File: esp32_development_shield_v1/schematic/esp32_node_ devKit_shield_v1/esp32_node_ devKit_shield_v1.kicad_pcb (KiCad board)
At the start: 2 copper layers, 150 x 80 mm, 41 parts, among them J1 Screw_Terminal_01x02, J10 Screw_Terminal_01x02, J11 Screw_Terminal_01x02, J12 Screw_Terminal_01x02, J13 Screw_Terminal_01x02, J14 Screw_Terminal_01x02, J15 Screw_Terminal_01x02, J16 Screw_Terminal_01x02, J17 Screw_Terminal_01x02, J19 Screw_Terminal_01x02, J2 Conn_02x20_Odd_Even, J20 Screw_Terminal_01x02, J21 Screw_Terminal_01x02, J22 Screw_Terminal_01x02, J23 Screw_Terminal_01x02, J24 Screw_Terminal_01x02, J25 Screw_Terminal_01x02, J26 Screw_Terminal_01x02, J27 Conn_01x04, J28 Conn_01x04, J29 Conn_01x04, J3 Conn_02x20_Odd_Even, J30 Conn_01x04, J31 USB_C_Receptacle_PowerOnly_6P, J4 Conn_01x04, J5 Conn_01x04, J6 Conn_01x04, J7 Conn_01x04, J8 Screw_Terminal_01x02, J9 Screw_Terminal_01x02, U2 AMS1117-3.3

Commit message: *
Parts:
- added J18: Conn_01x18_Pin, Connector_PinSocket_2.54mm:PinSocket_1x18_P2.54mm_Vertical, F.Cu at (116.3, 112.0)
- added J32: Conn_01x18_Pin, Connector_PinSocket_2.54mm:PinSocket_1x18_P2.54mm_Vertical, F.Cu at (116.3, 68.0)
- J2, J3: value Conn_02x20_Odd_Even -> Conn_02x19_Odd_Even; footprint Connector_PinSocket_2.54mm:PinSocket_2x20_P2.54mm_Vertical -> Connector_PinSocket_2.54mm:PinSocket_2x19_P2.54mm_Vertical
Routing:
- net /5V: track 269.3 -> 315.1 mm
- net GND: track 442.1 -> 414.4 mm
- net Net-(J18-Pin_16): track 52.1 -> 79.7 mm
- net Net-(J15-Pin_2): track 30.1 -> 41.4 mm
- net Net-(J15-Pin_1): track 28.6 -> 38.2 mm
- net Net-(J18-Pin_15): track 26.7 -> 36.2 mm
- net Net-(J14-Pin_2): track 26.6 -> 33.3 mm
- net Net-(J18-Pin_14): track 24.7 -> 31.3 mm
- net Net-(J3-Pin_10): track 33.0 -> 38.4 mm
- net Net-(J3-Pin_5): track 40.4 -> 45.6 mm
- net Net-(J18-Pin_13): track 23.6 -> 28.8 mm
- net Net-(J14-Pin_1): track 25.5 -> 30.7 mm
- net Net-(J3-Pin_7): track 35.5 -> 40.4 mm
- net Net-(J3-Pin_3): track 43.0 -> 47.5 mm
- net Net-(J10-Pin_1): track 28.8 -> 32.6 mm
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
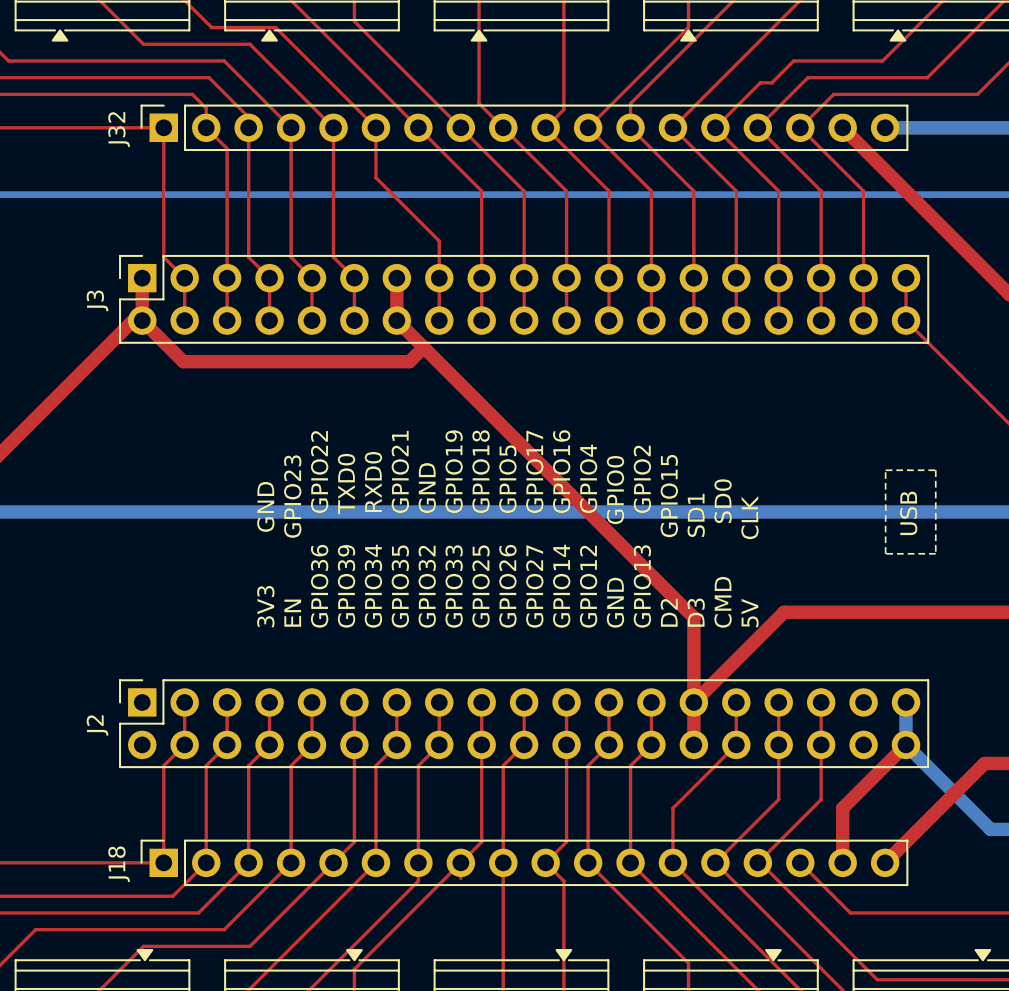
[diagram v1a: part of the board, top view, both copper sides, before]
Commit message: *
Replaced socket with header
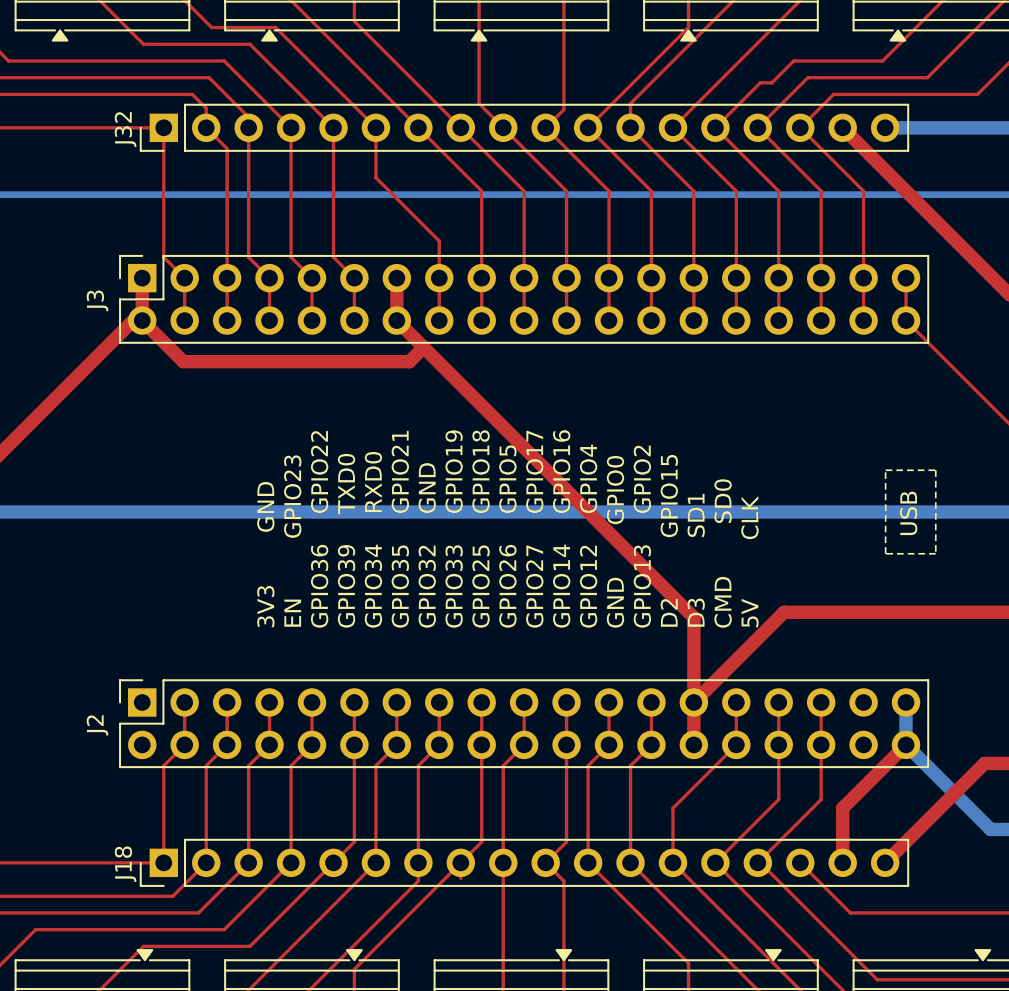
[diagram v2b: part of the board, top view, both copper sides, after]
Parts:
- J18, J32: footprint Connector_PinSocket_2.54mm:PinSocket_1x18_P2.54mm_Vertical -> Connector_PinHeader_2.54mm:PinHeader_1x18_P2.54mm_Vertical
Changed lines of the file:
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@@
 		)
 	)
-	(footprint "Connector_PinSocket_2.54mm:PinSocket_1x18_P2.54mm_Vertical"
+	(footprint "Connector_PinHeader_2.54mm:PinHeader_1x18_P2.54mm_Vertical"
 		(layer "F.Cu")
 		(at 116.29 68 90)
-		(descr "Through hole straight socket strip, 1x18, 2.54mm pitch, single row (from Kicad 4.0.7), script generated")
-		(tags "Through hole socket strip THT 1x18 2.54mm single row")
+		(descr "Through hole straight pin header, 1x18, 2.54mm pitch, single row")
+		(tags "Through hole pin header THT 1x18 2.54mm single row")
 		(property "Reference" "J32"
-			(at 0 -2.77 90)
+			(at 0 -2.38 90)
 			(layer "F.SilkS")
 			(effects
@@
 		)
 		(property "Value" "Conn_01x18_Pin"
-			(at 0 45.95 90)
+			(at 0 45.56 90)
 			(layer "F.Fab")
 			(effects
@@
 		(duplicate_pad_numbers_are_jumpers no)
 		(fp_line
-			(start 1.33 -1.33)
-			(end 1.33 0)
-			(stroke
-				(width 0.12)
-				(type solid)
-			)
-			(layer "F.SilkS")
-		)
-		(fp_line
-			(start 0 -1.33)
-			(end 1.33 -1.33)
-			(stroke
-				(width 0.12)
-				(type solid)
-			)
-			(layer "F.SilkS")
-		)
-		(fp_line
-			(start 1.33 1.27)
-			(end 1.33 44.51)
-			(stroke
-				(width 0.12)
-				(type solid)
-			)
-			(layer "F.SilkS")
-		)
-		(fp_line
-			(start -1.33 1.27)
-			(end 1.33 1.27)
-			(stroke
-				(width 0.12)
-				(type solid)
-			)
-			(layer "F.SilkS")
-		)
-		(fp_line
-			(start -1.33 1.27)
-			(end -1.33 44.51)
-			(stroke
-				(width 0.12)
-				(type solid)
-			)
-			(layer "F.SilkS")
-		)
-		(fp_line
-			(start -1.33 44.51)
-			(end 1.33 44.51)
-			(stroke
-				(width 0.12)
-				(type solid)
-			)
-			(layer "F.SilkS")
-		)
-		(fp_line
-			(start 1.77 -1.77)
+			(start -1.38 -1.38)
+			(end 0 -1.38)
+			(stroke
+				(width 0.12)
+				(type solid)
+			)
+			(layer "F.SilkS")
+		)
+		(fp_line
+			(start -1.38 0)
+			(end -1.38 -1.38)
+			(stroke
+				(width 0.12)
+				(type solid)
+			)
+			(layer "F.SilkS")
+		)
+		(fp_line
+			(start 1.38 1.27)
+			(end 1.38 44.56)
+			(stroke
+				(width 0.12)
+				(type solid)
+			)
+			(layer "F.SilkS")
+		)
+		(fp_line
+			(start -1.38 1.27)
+			(end 1.38 1.27)
+			(stroke
+				(width 0.12)
+				(type solid)
+			)
+			(layer "F.SilkS")
+		)
+		(fp_line
+			(start -1.38 1.27)
+			(end -1.38 44.56)
+			(stroke
+				(width 0.12)
+				(type solid)
+			)
+			(layer "F.SilkS")
+		)
+		(fp_line
+			(start -1.38 44.56)
+			(end 1.38 44.56)
+			(stroke
+				(width 0.12)
+				(type solid)
+			)
+			(layer "F.SilkS")
+		)
+		(fp_rect
+			(start -1.77 -1.78)
 			(end 1.77 44.95)
 			(stroke
@@
 				(type solid)
 			)
+			(fill no)
 			(layer "F.CrtYd")
 		)
 		(fp_line
-			(start -1.77 -1.77)
-			(end 1.77 -1.77)
-			(stroke
-				(width 0.05)
-				(type solid)
-			)
-			(layer "F.CrtYd")
-		)
-		(fp_line
-			(start 1.77 44.95)
-			(end -1.77 44.95)
-			(stroke
-				(width 0.05)
-				(type solid)
-			)
-			(layer "F.CrtYd")
-		)
-		(fp_line
-			(start -1.77 44.95)
-			(end -1.77 -1.77)
-			(stroke
-				(width 0.05)
-				(type solid)
-			)
-			(layer "F.CrtYd")
-		)
-		(fp_line
-			(start 0.635 -1.27)
-			(end 1.27 -0.635)
-			(stroke
-				(width 0.1)
-				(type solid)
-			)
-			(layer "F.Fab")
-		)
-		(fp_line
-			(start -1.27 -1.27)
-			(end 0.635 -1.27)
-			(stroke
-				(width 0.1)
-				(type solid)
-			)
-			(layer "F.Fab")
-		)
-		(fp_line
-			(start 1.27 -0.635)
+			(start 1.27 -1.27)
 			(end 1.27 44.45)
+			(stroke
+				(width 0.1)
+				(type solid)
+			)
+			(layer "F.Fab")
+		)
+		(fp_line
+			(start -0.635 -1.27)
+			(end 1.27 -1.27)
+			(stroke
+				(width 0.1)
+				(type solid)
+			)
+			(layer "F.Fab")
+		)
+		(fp_line
+			(start -1.27 -0.635)
+			(end -0.635 -1.27)
 			(stroke
 				(width 0.1)
@@
 		(fp_line
 			(start -1.27 44.45)
-			(end -1.27 -1.27)
+			(end -1.27 -0.635)
 			(stroke
 				(width 0.1)
@@
 		)
 		(fp_text user "${REFERENCE}"
-			(at 0 21.59 0)
+			(at 0 21.59 180)
 			(layer "F.Fab")
 			(effects
@@
 		)
 		(embedded_fonts no)
-		(model "${KICAD10_3DMODEL_DIR}/Connector_PinSocket_2.54mm.3dshapes/PinSocket_1x18_P2.54mm_Vertical.step"
+		(model "${KICAD10_3DMODEL_DIR}/Connector_PinHeader_2.54mm.3dshapes/PinHeader_1x18_P2.54mm_Vertical.step"
 			(offset
 				(xyz 0 0 0)
@@
 		(embedded_fonts no)
 	)
-	(footprint "Connector_PinSocket_2.54mm:PinSocket_1x18_P2.54mm_Vertical"
+	(footprint "Connector_PinHeader_2.54mm:PinHeader_1x18_P2.54mm_Vertical"
 		(layer "F.Cu")
 		(at 116.29 112 90)
-		(descr "Through hole straight socket strip, 1x18, 2.54mm pitch, single row (from Kicad 4.0.7), script generated")
-		(tags "Through hole socket strip THT 1x18 2.54mm single row")
+		(descr "Through hole straight pin header, 1x18, 2.54mm pitch, single row")
+		(tags "Through hole pin header THT 1x18 2.54mm single row")
 		(property "Reference" "J18"
-			(at 0 -2.77 90)
+			(at 0 -2.38 90)
 			(layer "F.SilkS")
 			(effects
@@
 		)
 		(property "Value" "Conn_01x18_Pin"
-			(at 0 45.95 90)
+			(at 0 45.56 90)
 			(layer "F.Fab")
 			(effects
@@
 		(duplicate_pad_numbers_are_jumpers no)
 		(fp_line
-			(start 1.33 -1.33)
-			(end 1.33 0)
-			(stroke
-				(width 0.12)
-				(type solid)
-			)
-			(layer "F.SilkS")
-		)
-		(fp_line
-			(start 0 -1.33)
-			(end 1.33 -1.33)
-			(stroke
-				(width 0.12)
-				(type solid)
-			)
-			(layer "F.SilkS")
-		)
-		(fp_line
-			(start 1.33 1.27)
-			(end 1.33 44.51)
-			(stroke
-				(width 0.12)
-				(type solid)
-			)
-			(layer "F.SilkS")
-		)
-		(fp_line
-			(start -1.33 1.27)
-			(end 1.33 1.27)
-			(stroke
-				(width 0.12)
-				(type solid)
-			)
-			(layer "F.SilkS")
-		)
-		(fp_line
-			(start -1.33 1.27)
-			(end -1.33 44.51)
-			(stroke
-				(width 0.12)
-				(type solid)
-			)
-			(layer "F.SilkS")
-		)
-		(fp_line
-			(start -1.33 44.51)
-			(end 1.33 44.51)
-			(stroke
-				(width 0.12)
-				(type solid)
-			)
-			(layer "F.SilkS")
-		)
-		(fp_line
-			(start 1.77 -1.77)
+			(start -1.38 -1.38)
+			(end 0 -1.38)
+			(stroke
+				(width 0.12)
+				(type solid)
+			)
+			(layer "F.SilkS")
+		)
+		(fp_line
+			(start -1.38 0)
+			(end -1.38 -1.38)
+			(stroke
+				(width 0.12)
+				(type solid)
+			)
+			(layer "F.SilkS")
+		)
+		(fp_line
+			(start 1.38 1.27)
+			(end 1.38 44.56)
+			(stroke
+				(width 0.12)
+				(type solid)
+			)
+			(layer "F.SilkS")
+		)
+		(fp_line
+			(start -1.38 1.27)
+			(end 1.38 1.27)
+			(stroke
+				(width 0.12)
+				(type solid)
+			)
+			(layer "F.SilkS")
+		)
+		(fp_line
+			(start -1.38 1.27)
+			(end -1.38 44.56)
+			(stroke
+				(width 0.12)
+				(type solid)
+			)
+			(layer "F.SilkS")
+		)
+		(fp_line
+			(start -1.38 44.56)
+			(end 1.38 44.56)
+			(stroke
+				(width 0.12)
+				(type solid)
+			)
+			(layer "F.SilkS")
+		)
+		(fp_rect
+			(start -1.77 -1.78)
 			(end 1.77 44.95)
 			(stroke
@@
 				(type solid)
 			)
+			(fill no)
 			(layer "F.CrtYd")
 		)
 		(fp_line
-			(start -1.77 -1.77)
-			(end 1.77 -1.77)
-			(stroke
-				(width 0.05)
-				(type solid)
-			)
-			(layer "F.CrtYd")
-		)
-		(fp_line
-			(start 1.77 44.95)
-			(end -1.77 44.95)
-			(stroke
-				(width 0.05)
-				(type solid)
-			)
-			(layer "F.CrtYd")
-		)
-		(fp_line
-			(start -1.77 44.95)
-			(end -1.77 -1.77)
-			(stroke
-				(width 0.05)
-				(type solid)
-			)
-			(layer "F.CrtYd")
-		)
-		(fp_line
-			(start 0.635 -1.27)
-			(end 1.27 -0.635)
-			(stroke
-				(width 0.1)
-				(type solid)
-			)
-			(layer "F.Fab")
-		)
-		(fp_line
-			(start -1.27 -1.27)
-			(end 0.635 -1.27)
-			(stroke
-				(width 0.1)
-				(type solid)
-			)
-			(layer "F.Fab")
-		)
-		(fp_line
-			(start 1.27 -0.635)
+			(start 1.27 -1.27)
 			(end 1.27 44.45)
+			(stroke
+				(width 0.1)
+				(type solid)
+			)
+			(layer "F.Fab")
+		)
+		(fp_line
+			(start -0.635 -1.27)
+			(end 1.27 -1.27)
+			(stroke
+				(width 0.1)
+				(type solid)
+			)
+			(layer "F.Fab")
+		)
+		(fp_line
+			(start -1.27 -0.635)
+			(end -0.635 -1.27)
 			(stroke
 				(width 0.1)
@@
 		(fp_line
 			(start -1.27 44.45)
-			(end -1.27 -1.27)
+			(end -1.27 -0.635)
 			(stroke
 				(width 0.1)
@@
 		)
 		(fp_text user "${REFERENCE}"
-			(at 0 21.59 0)
+			(at 0 21.59 180)
 			(layer "F.Fab")
 			(effects
@@
 		)
 		(embedded_fonts no)
-		(model "${KICAD10_3DMODEL_DIR}/Connector_PinSocket_2.54mm.3dshapes/PinSocket_1x18_P2.54mm_Vertical.step"
+		(model "${KICAD10_3DMODEL_DIR}/Connector_PinHeader_2.54mm.3dshapes/PinHeader_1x18_P2.54mm_Vertical.step"
 			(offset
 				(xyz 0 0 0)

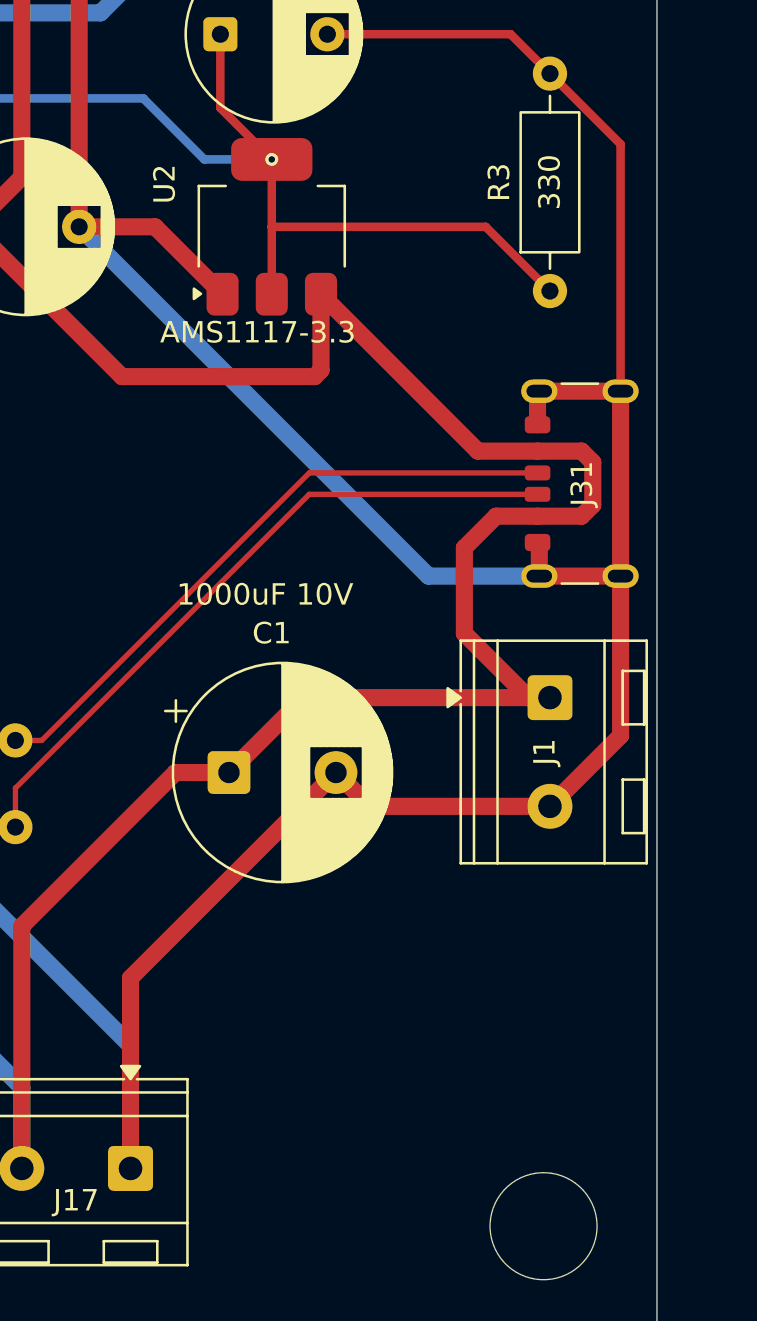
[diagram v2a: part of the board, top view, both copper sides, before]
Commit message: Added LED for power on/off
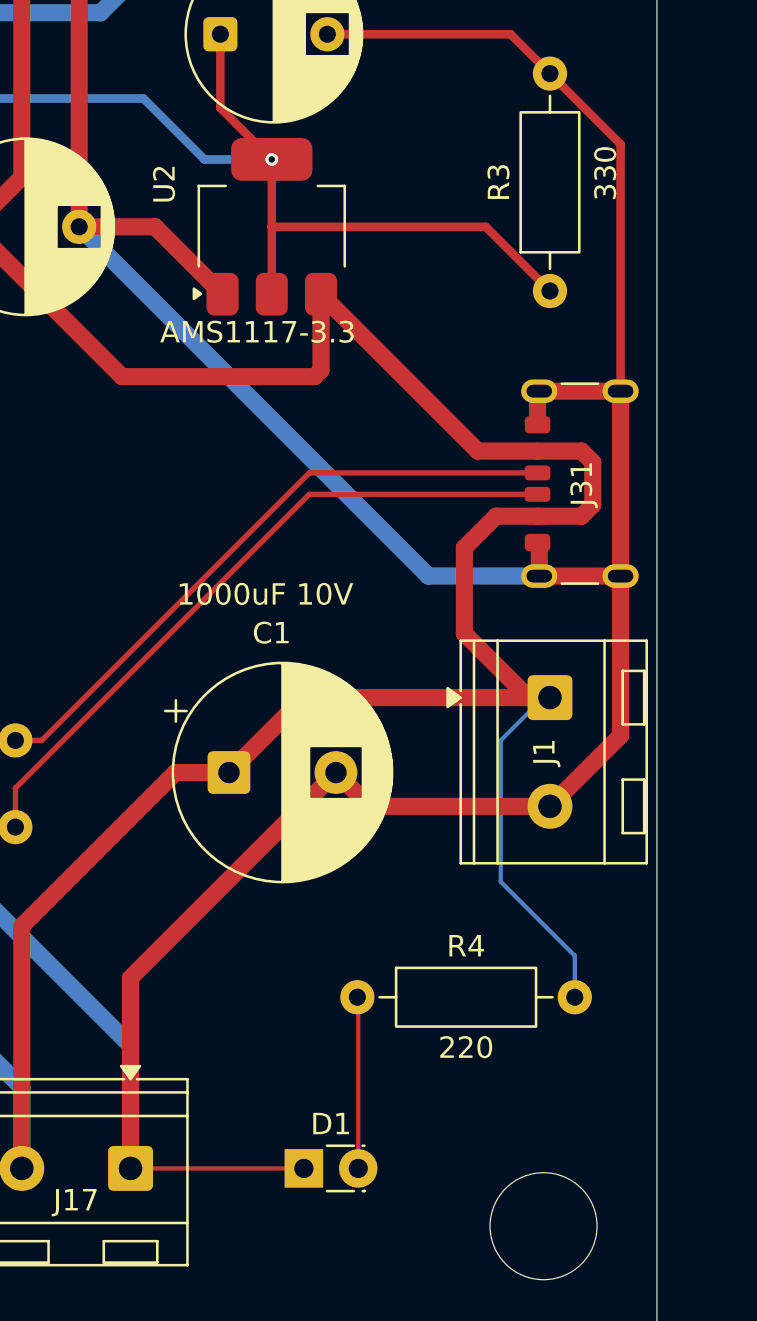
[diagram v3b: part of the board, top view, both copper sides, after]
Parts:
- added D1: LED, LED_THT:LED_Rectangular_W3.0mm_H2.0mm, F.Cu at (198.5, 122.0)
- added R4: 220, Resistor_THT:R_Axial_DIN0207_L6.3mm_D2.5mm_P10.16mm_Horizontal, F.Cu at (201.0, 114.0)
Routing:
- net /5V: track 315.1 -> 331.7 mm
- net GND: track 414.4 -> 422.5 mm
- net Net-(D1-A): track 0.00 -> 8.02 mm
